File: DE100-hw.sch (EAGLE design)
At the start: 51 parts, among them IC3 74HC14D, IC4 74HC14D, U1 TLP521-4(GB), U2 TLP521-4(GB), X1 22-23-2041, X2 22-23-2031, X3 22-23-2101

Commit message: post production revision
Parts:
- R1, R10, R11, R18, R2, R26, R27, R3, R4, R9: value (none) -> 330
- R12, R13, R14, R5, R6, R7, R8: value (none) -> 10k
- R15, R16, R17, R19, R20, R21, R22, R23, R24, R25: value (none) -> 1k

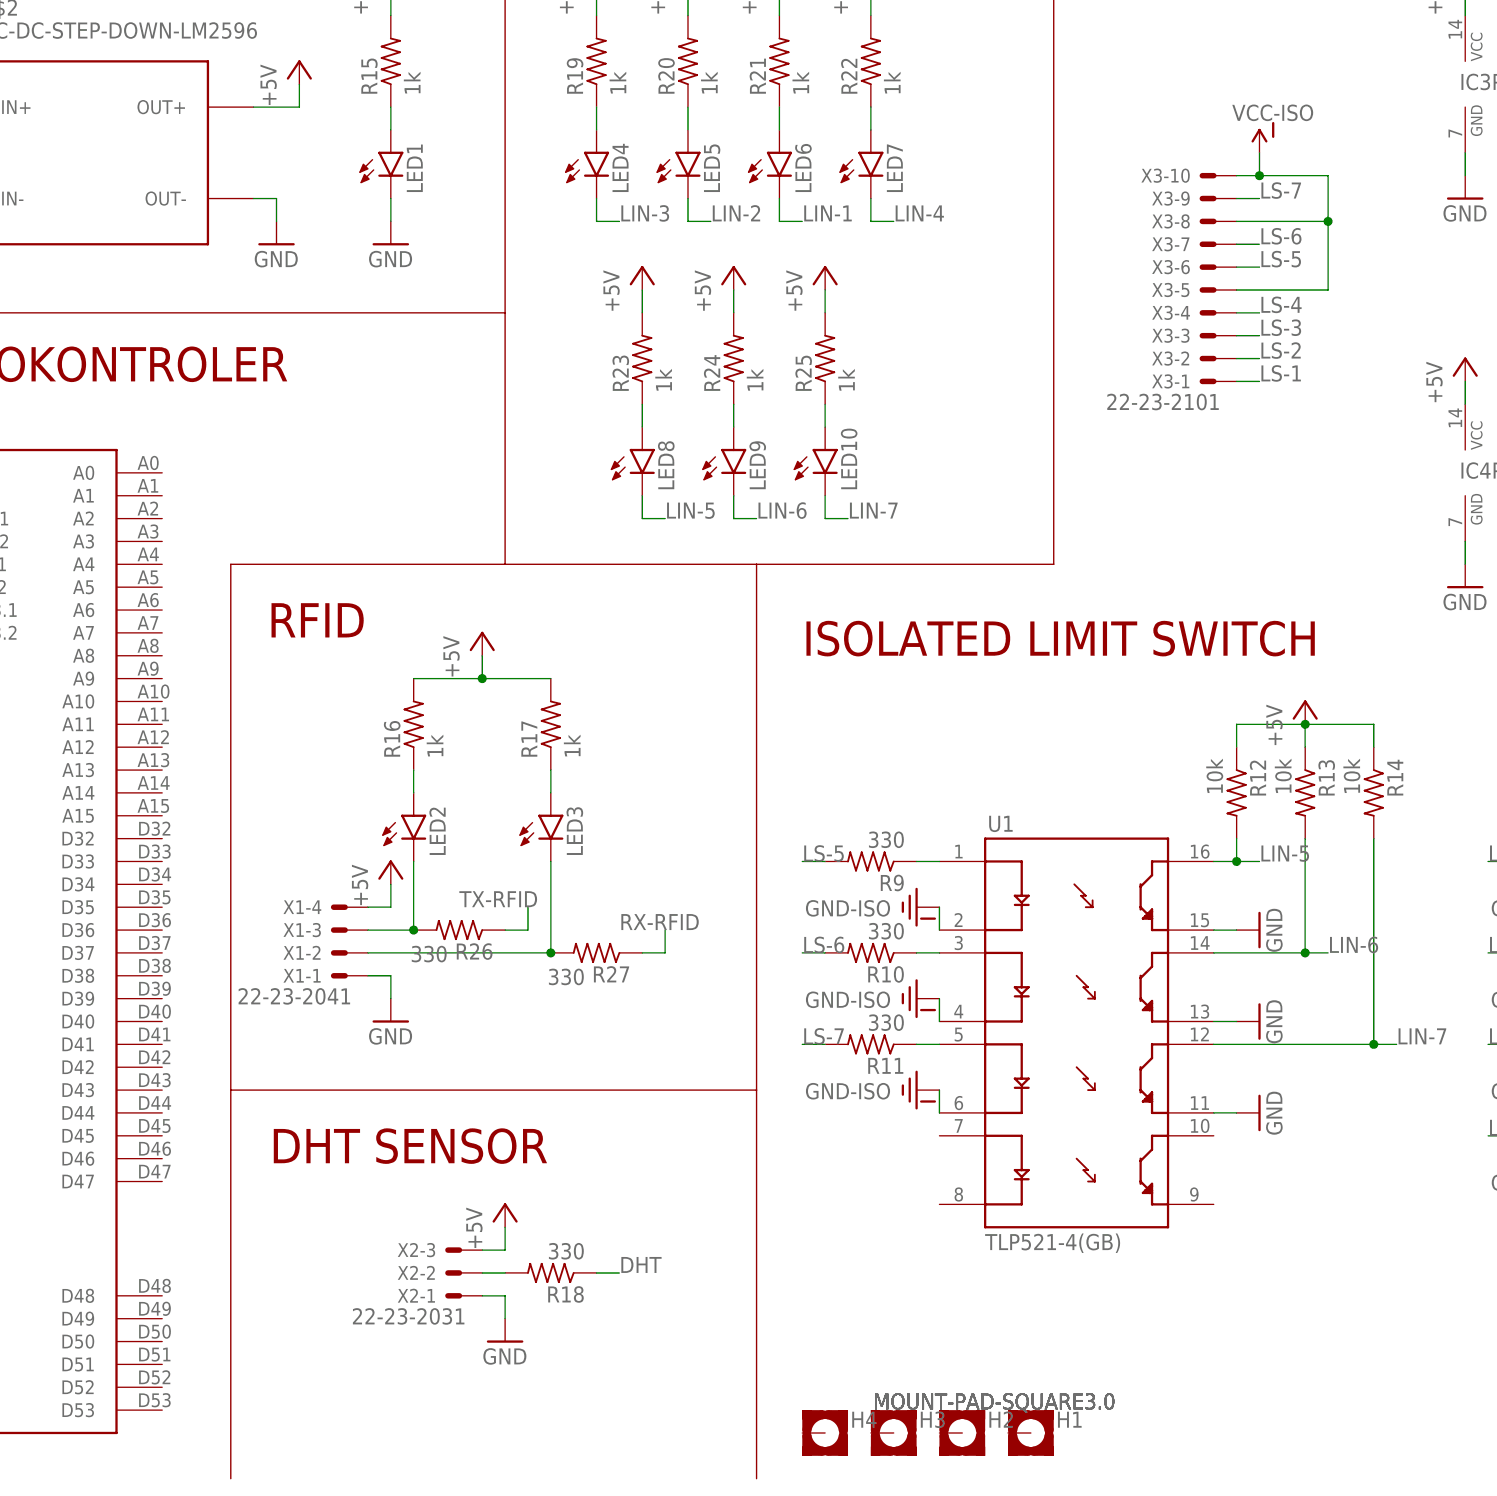
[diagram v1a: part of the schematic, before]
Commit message: change molex connector library
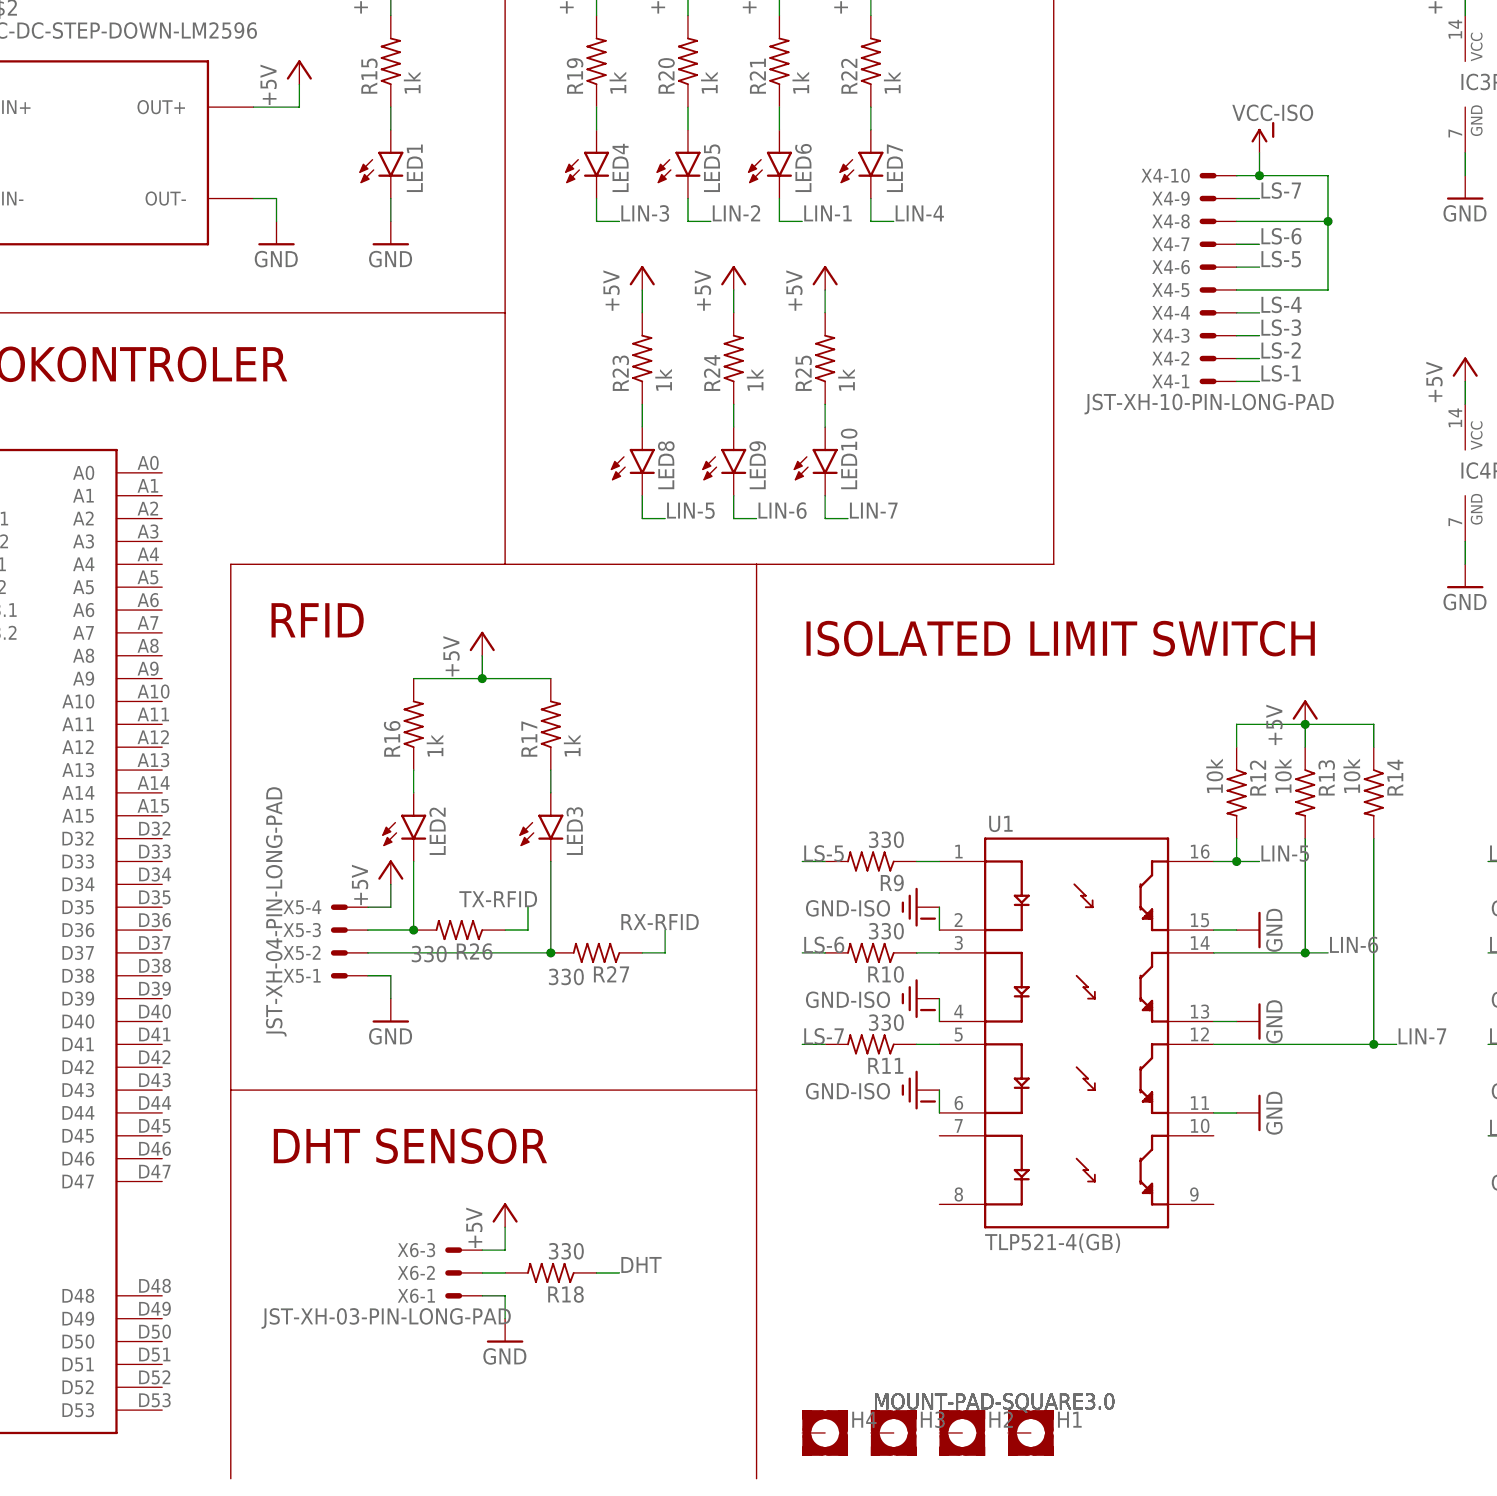
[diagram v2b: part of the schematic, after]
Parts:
- removed X1: 22-23-2041, con-molex:22-23-2041
- removed X2: 22-23-2031, con-molex:22-23-2031
- removed X3: 22-23-2101, con-molex:22-23-2101
- added X4: JST-XH-10-PIN-LONG-PAD, Rembrandt Electronics - JST XH Connectors v1-0:JST-XH-10-PIN-LONG-PAD
- added X5: JST-XH-04-PIN-LONG-PAD, Rembrandt Electronics - JST XH Connectors v1-0:JST-XH-04-PIN-LONG-PAD
- added X6: JST-XH-03-PIN-LONG-PAD, Rembrandt Electronics - JST XH Connectors v1-0:JST-XH-03-PIN-LONG-PAD
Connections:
- net +5V: now also X5-4.S, X6-3.S; no longer X1-4.S, X2-3.S
- net GND: now also X5-1.S, X6-1.S; no longer X1-1.S, X2-1.S
- net LS-1: now also X4-1.S; no longer X3-1.S
- net LS-2: now also X4-2.S; no longer X3-2.S
- net LS-3: now also X4-3.S; no longer X3-3.S
- net LS-4: now also X4-4.S; no longer X3-4.S
- net LS-5: now also X4-6.S; no longer X3-6.S
- net LS-6: now also X4-7.S; no longer X3-7.S
- net LS-7: now also X4-9.S; no longer X3-9.S
- net N$35: now also X5-3.S; no longer X1-3.S
- net N$36: now also X5-2.S; no longer X1-2.S
- net N$38: now also X6-2.S; no longer X2-2.S
- net VCC-ISO: now also X4-10.S, X4-5.S, X4-8.S; no longer X3-10.S, X3-5.S, X3-8.S

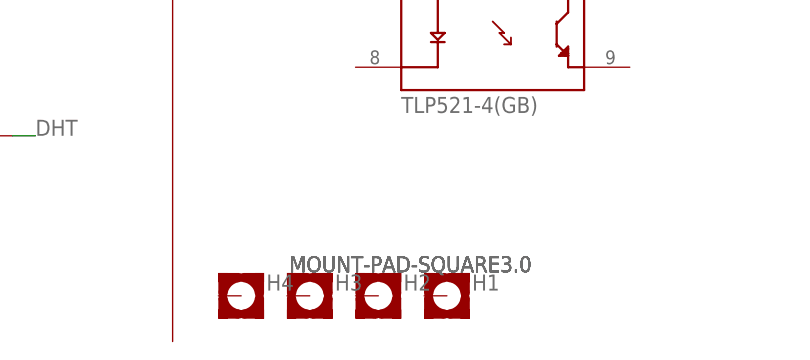
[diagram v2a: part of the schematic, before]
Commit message: change position component and logo HM
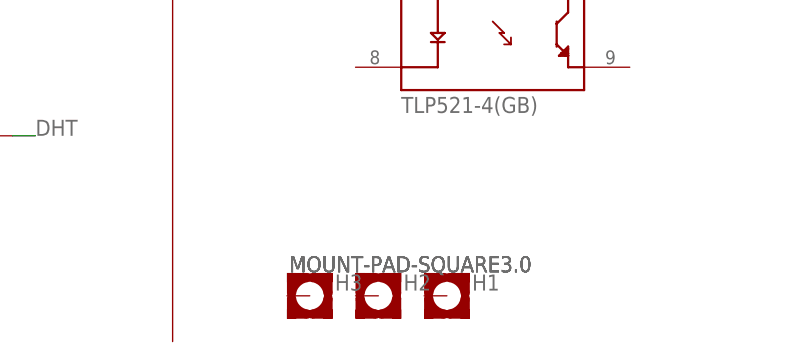
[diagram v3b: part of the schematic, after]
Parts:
- removed H4: MOUNT-PAD-SQUARE3.0, holes:MOUNT-PAD-SQUARE3.0
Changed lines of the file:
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@@
 <part name="H2" library="holes" library_urn="urn:adsk.eagle:library:237" deviceset="MOUNT-PAD-SQUARE" device="3.0" package3d_urn="urn:adsk.eagle:package:14290/1"/>
 <part name="H3" library="holes" library_urn="urn:adsk.eagle:library:237" deviceset="MOUNT-PAD-SQUARE" device="3.0" package3d_urn="urn:adsk.eagle:package:14290/1"/>
-<part name="H4" library="holes" library_urn="urn:adsk.eagle:library:237" deviceset="MOUNT-PAD-SQUARE" device="3.0" package3d_urn="urn:adsk.eagle:package:14290/1"/>
 <part name="X4" library="Rembrandt Electronics - JST XH Connectors v1-0" deviceset="JST-XH-10-PIN" device="-LONG-PAD"/>
 <part name="X5" library="Rembrandt Electronics - JST XH Connectors v1-0" deviceset="JST-XH-04-PIN" device="-LONG-PAD"/>
@@
 <attribute name="VALUE" x="124.714" y="7.6962" size="1.778" layer="96"/>
 </instance>
-<instance part="H4" gate="G$1" x="119.38" y="5.08" smashed="yes">
-<attribute name="NAME" x="122.174" y="5.6642" size="1.778" layer="95"/>
-<attribute name="VALUE" x="124.714" y="7.6962" size="1.778" layer="96"/>
-</instance>
